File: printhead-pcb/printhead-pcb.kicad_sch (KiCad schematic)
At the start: 30 parts, among them J1 Power, J2 DSCL, J3 DSDA, U1 PCA9615DP, U6 AP7361C-33E

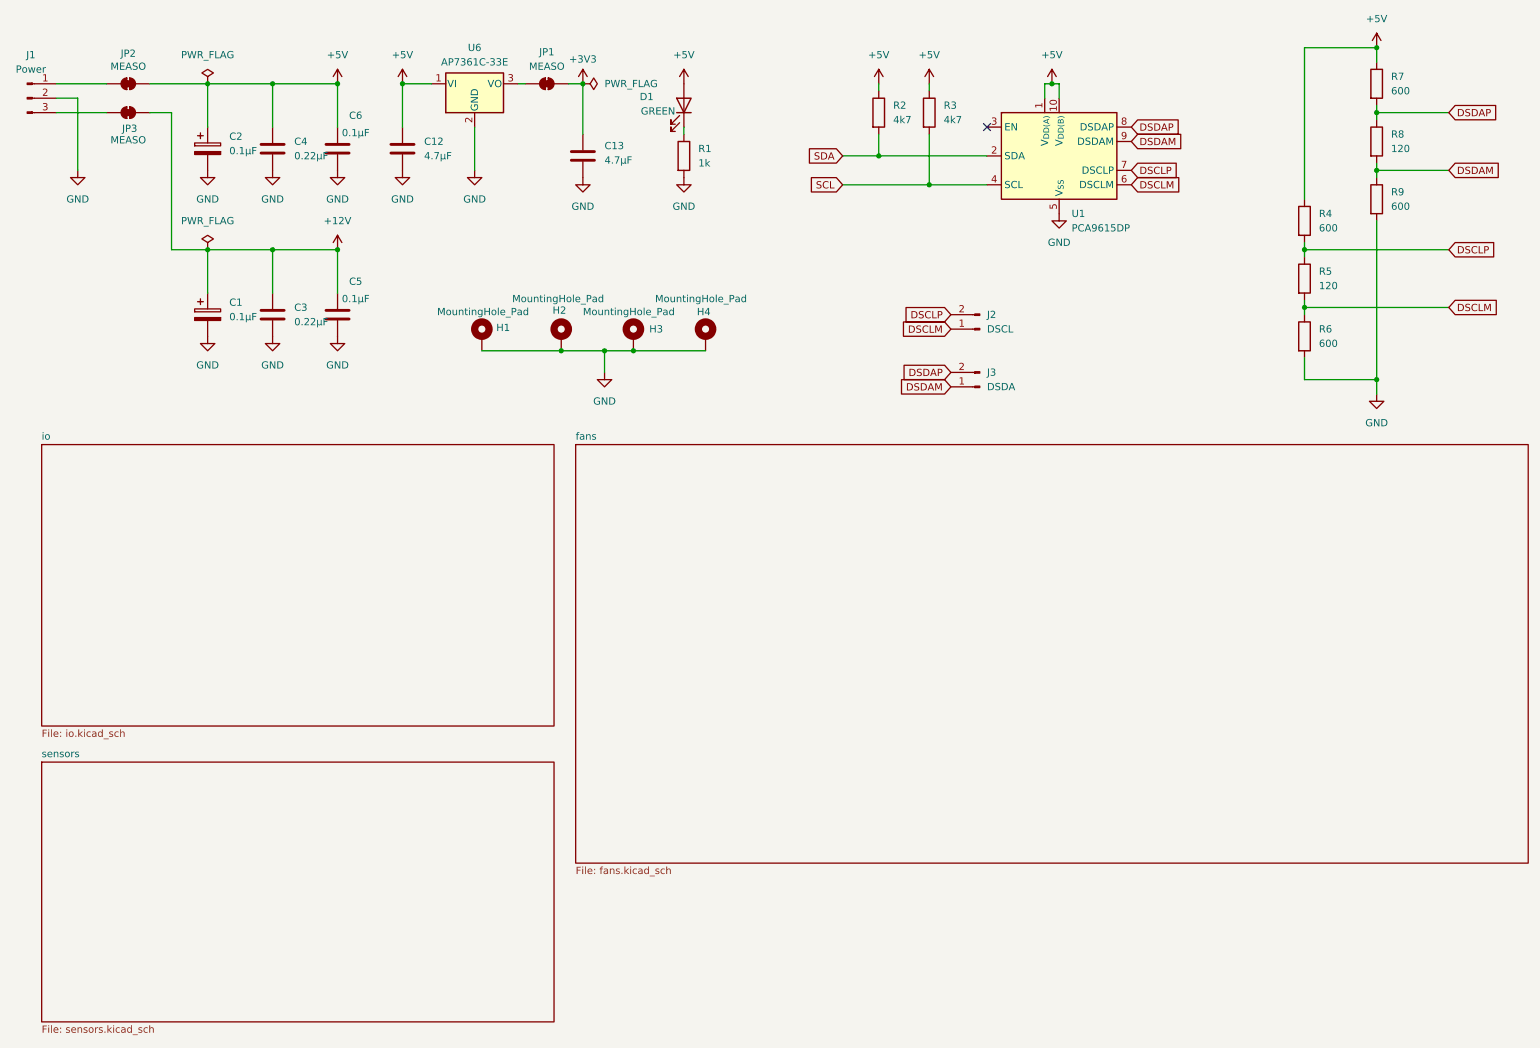
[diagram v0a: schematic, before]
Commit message: added LED Driver and servos
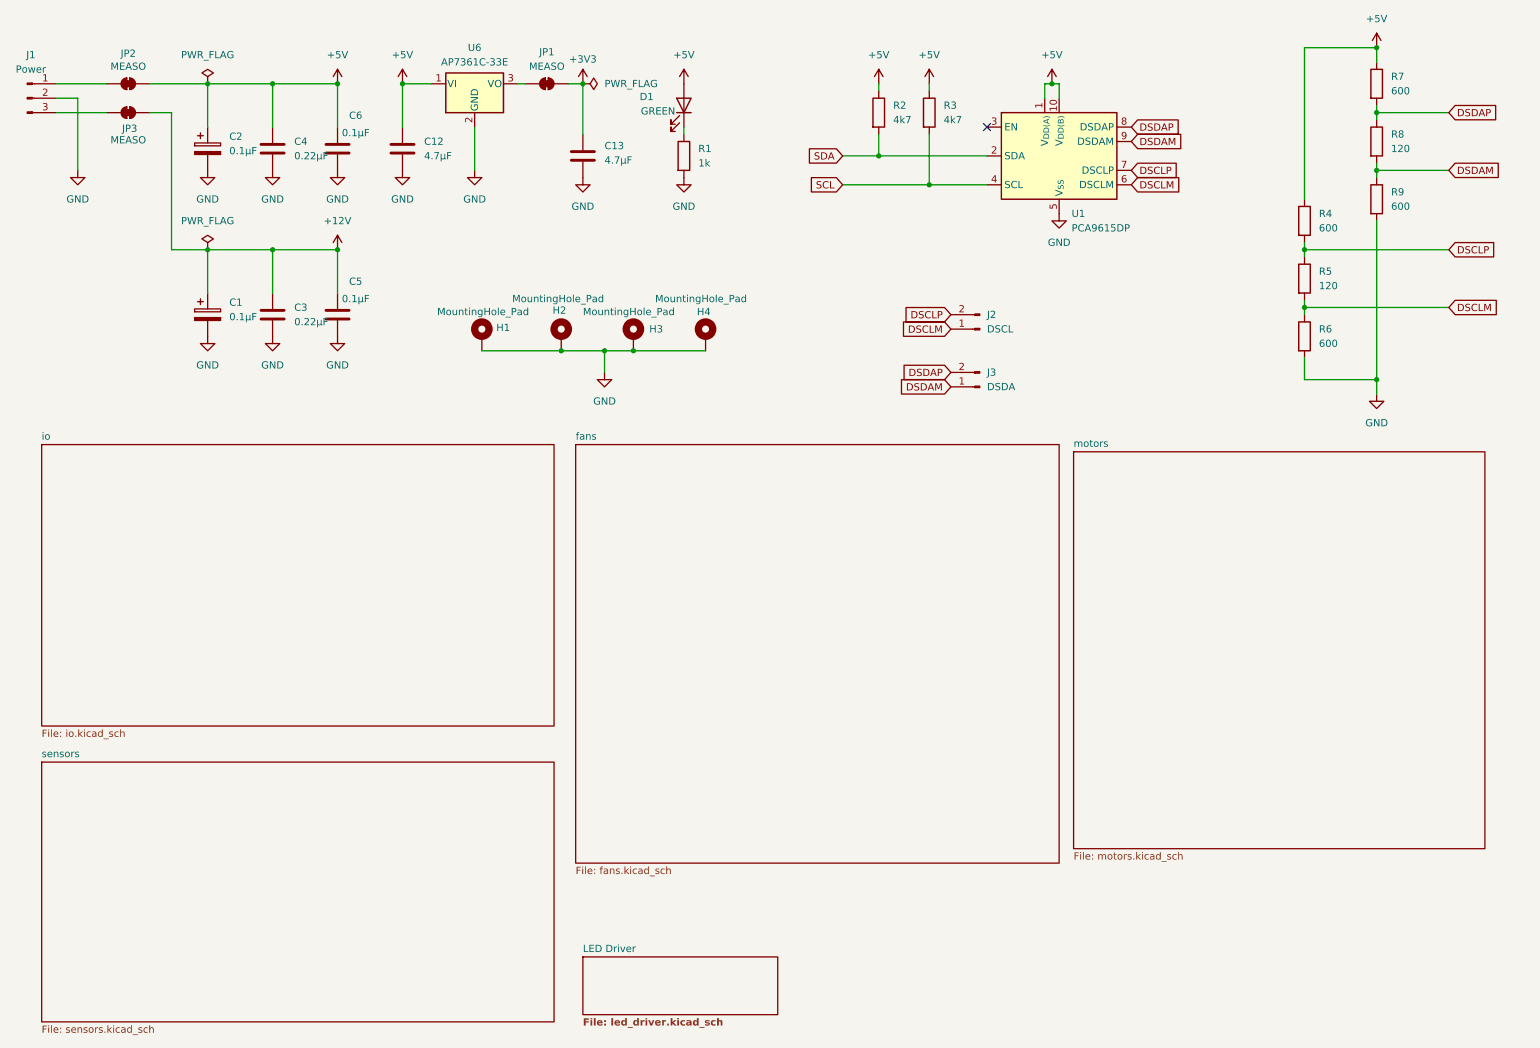
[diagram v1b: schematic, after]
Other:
- added sheet LED Driver (led_driver.kicad_sch)
- added sheet motors (motors.kicad_sch)
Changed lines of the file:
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@@
+	)
+	(sheet
+		(at 201.93 90.17)
+		(size 72.39 69.85)
+		(fields_autoplaced yes)
+		(stroke
+			(width 0.1524)
+			(type solid)
+		)
+		(fill
+			(color 0 0 0 0.0000)
+		)
+		(property "Sheetname" "motors"
+			(at 201.93 89.4584 0)
+			(effects
+				(font
+					(size 1.27 1.27)
+				)
+				(justify left bottom)
+			)
+		)
+		(property "Sheetfile" "motors.kicad_sch"
+			(at 201.93 160.6046 0)
+			(effects
+				(font
+					(size 1.27 1.27)
+				)
+				(justify left top)
+			)
+		)
+		(instances
+			(project "printhead-pcb"
+				(path "/813ad687-b864-44a5-b729-c4edf26b731d"
+					(page "6")
+				)
+			)
+		)
 	)
 	(sheet
 		(at 114.3 88.9)
-		(size 167.64 73.66)
+		(size 85.09 73.66)
 		(fields_autoplaced yes)
 		(stroke
@@
 				)
 			)
+		)
+	)
+	(sheet
+		(at 115.57 179.07)
+		(size 34.29 10.16)
+		(fields_autoplaced yes)
+		(stroke
+			(width 0.1524)
+			(type solid)
+		)
+		(fill
+			(color 0 0 0 0.0000)
+		)
+		(property "Sheetname" "LED Driver"
+			(at 115.57 178.3584 0)
+			(effects
+				(font
+					(size 1.27 1.27)
+				)
+				(justify left bottom)
+			)
+		)
+		(property "Sheetfile" "led_driver.kicad_sch"
+			(at 115.57 189.8146 0)
+			(effects
+				(font
+					(size 1.27 1.27)
+					(bold yes)
+				)
+				(justify left top)
+			)
+		)
+		(instances
+			(project "printhead-pcb"
+				(path "/813ad687-b864-44a5-b729-c4edf26b731d"
+					(page "5")
+				)
+			)

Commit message: Buchse für Netzwerk kabel hinzugefügt, LED Driver überarbeitet, gpio überarbeitet
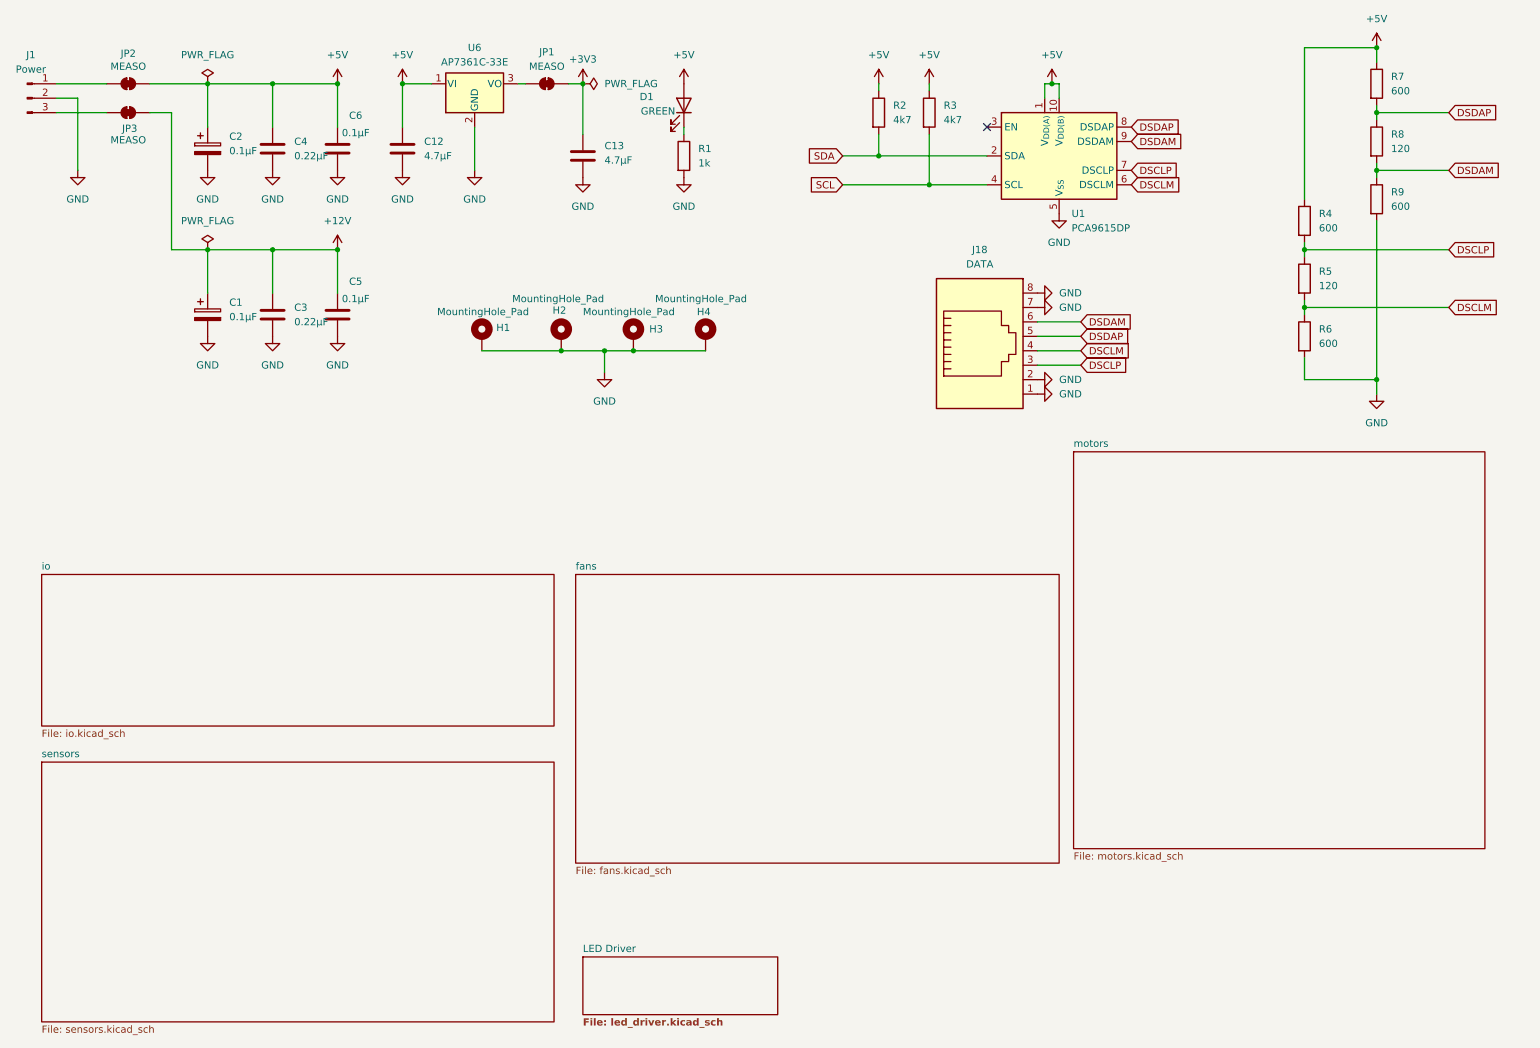
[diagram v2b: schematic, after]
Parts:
- removed J2: DSCL, symbol Connector:Conn_01x02_Pin
- removed J3: DSDA, symbol Connector:Conn_01x02_Pin
- added J18: DATA, Connector_RJ:RJ45_Amphenol_54602-x08_Horizontal, symbol Connector:RJ45
- J1: footprint (none) -> Connector_JST:JST_EH_S3B-EH_1x03_P2.50mm_Horizontal
- JP1, JP2, JP3: footprint (none) -> Jumper:SolderJumper-2_P1.3mm_Bridged_Pad1.0x1.5mm
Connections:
- net DSCLM: now also J18.4
- net DSCLP: now also J18.3
- net DSDAM: now also J18.6
- net DSDAP: now also J18.5
- net GND: now also J18.1, J18.2, J18.7, J18.8

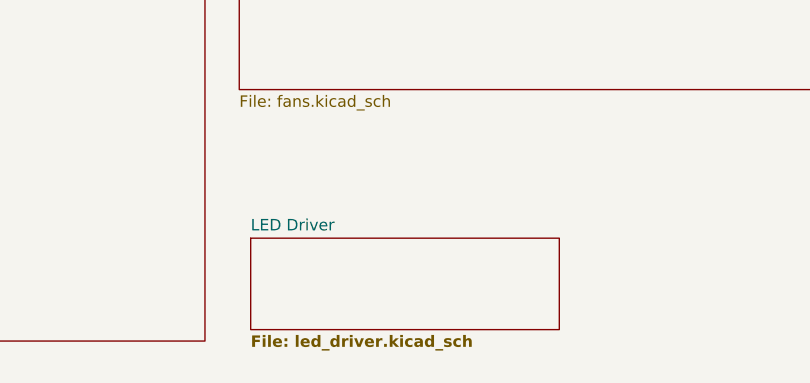
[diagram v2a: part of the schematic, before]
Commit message: removed led driver, added RJ45 (data connector), fan 3. 4. on off
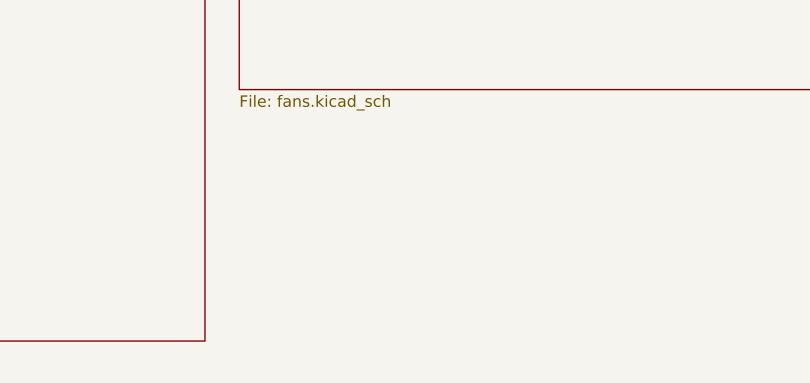
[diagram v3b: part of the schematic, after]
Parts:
- J18: footprint Connector_RJ:RJ45_Amphenol_54602-x08_Horizontal -> Connector_RJ:RJ45_Molex_0855135013_Vertical
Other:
- removed sheet LED Driver
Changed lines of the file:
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@@
 			)
 		)
-		(property "Footprint" "Connector_RJ:RJ45_Amphenol_54602-x08_Horizontal"
+		(property "Footprint" "Connector_RJ:RJ45_Molex_0855135013_Vertical"
 			(at 185.42 71.755 90)
 			(effects
@@
 				)
 			)
-		)
-	)
-	(sheet
-		(at 115.57 179.07)
-		(size 34.29 10.16)
-		(fields_autoplaced yes)
-		(stroke
-			(width 0.1524)
-			(type solid)
-		)
-		(fill
-			(color 0 0 0 0.0000)
-		)
-		(property "Sheetname" "LED Driver"
-			(at 115.57 178.3584 0)
-			(effects
-				(font
-					(size 1.27 1.27)
-				)
-				(justify left bottom)
-			)
-		)
-		(property "Sheetfile" "led_driver.kicad_sch"
-			(at 115.57 189.8146 0)
-			(effects
-				(font
-					(size 1.27 1.27)
-					(bold yes)
-				)
-				(justify left top)
-			)
-		)
-		(instances
-			(project "printhead-pcb"
-				(path "/813ad687-b864-44a5-b729-c4edf26b731d"
-					(page "5")
-				)
-			)

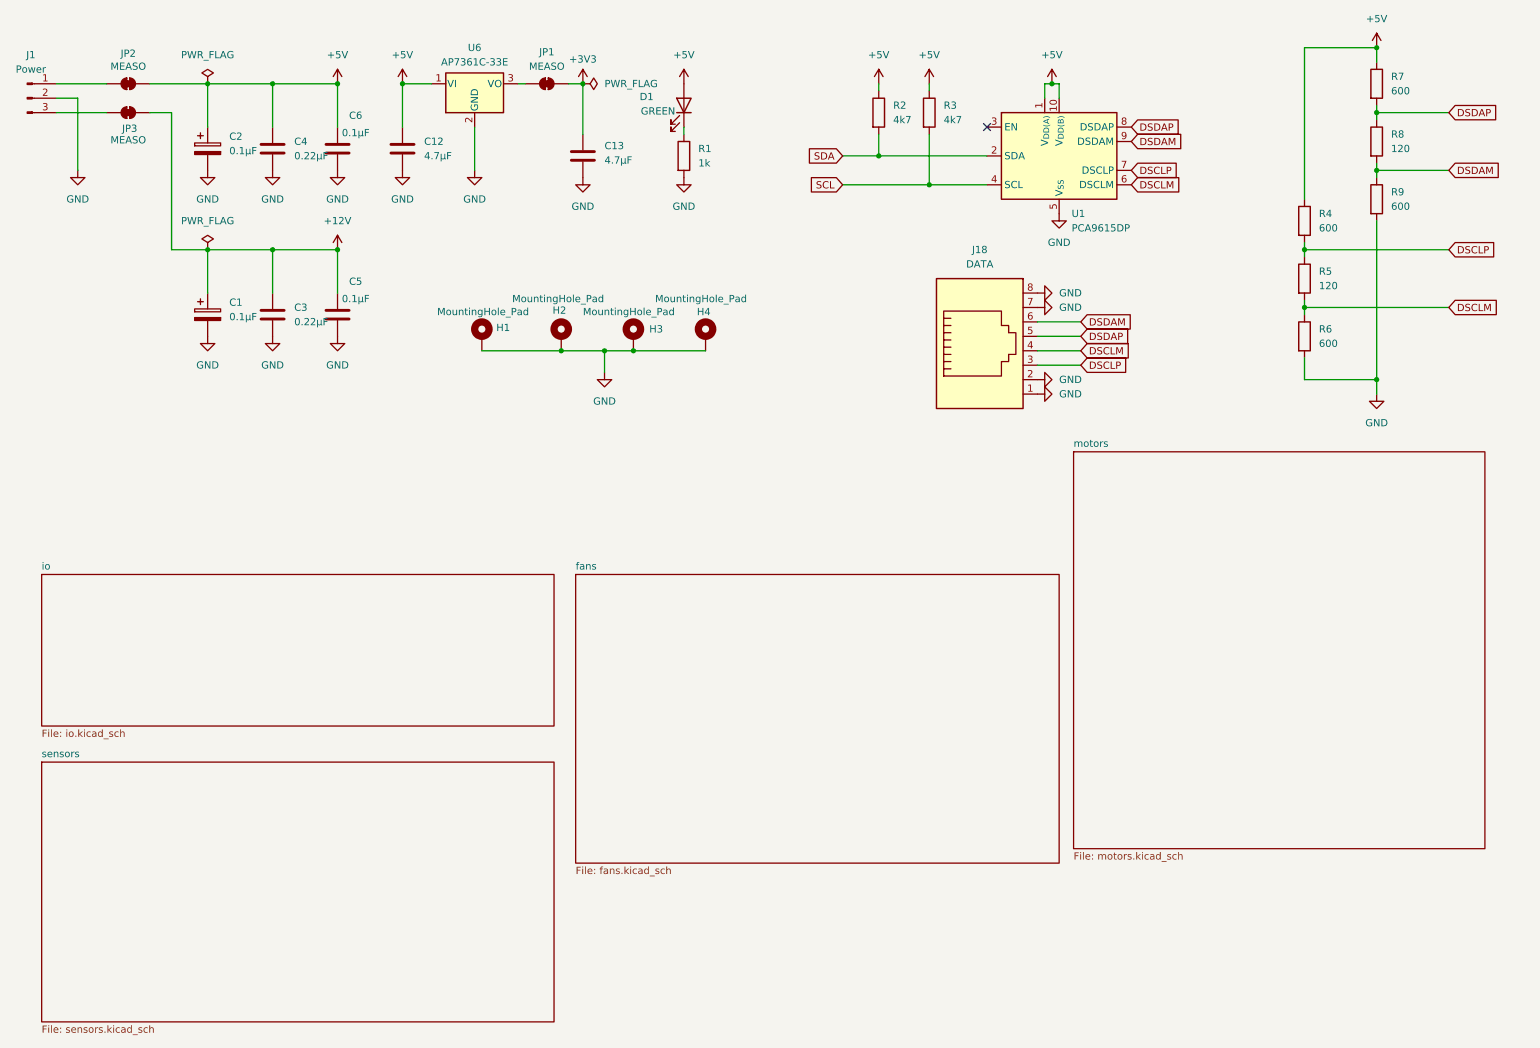
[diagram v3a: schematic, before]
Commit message: Beschriftungen im Schaltplan hinzugefügt
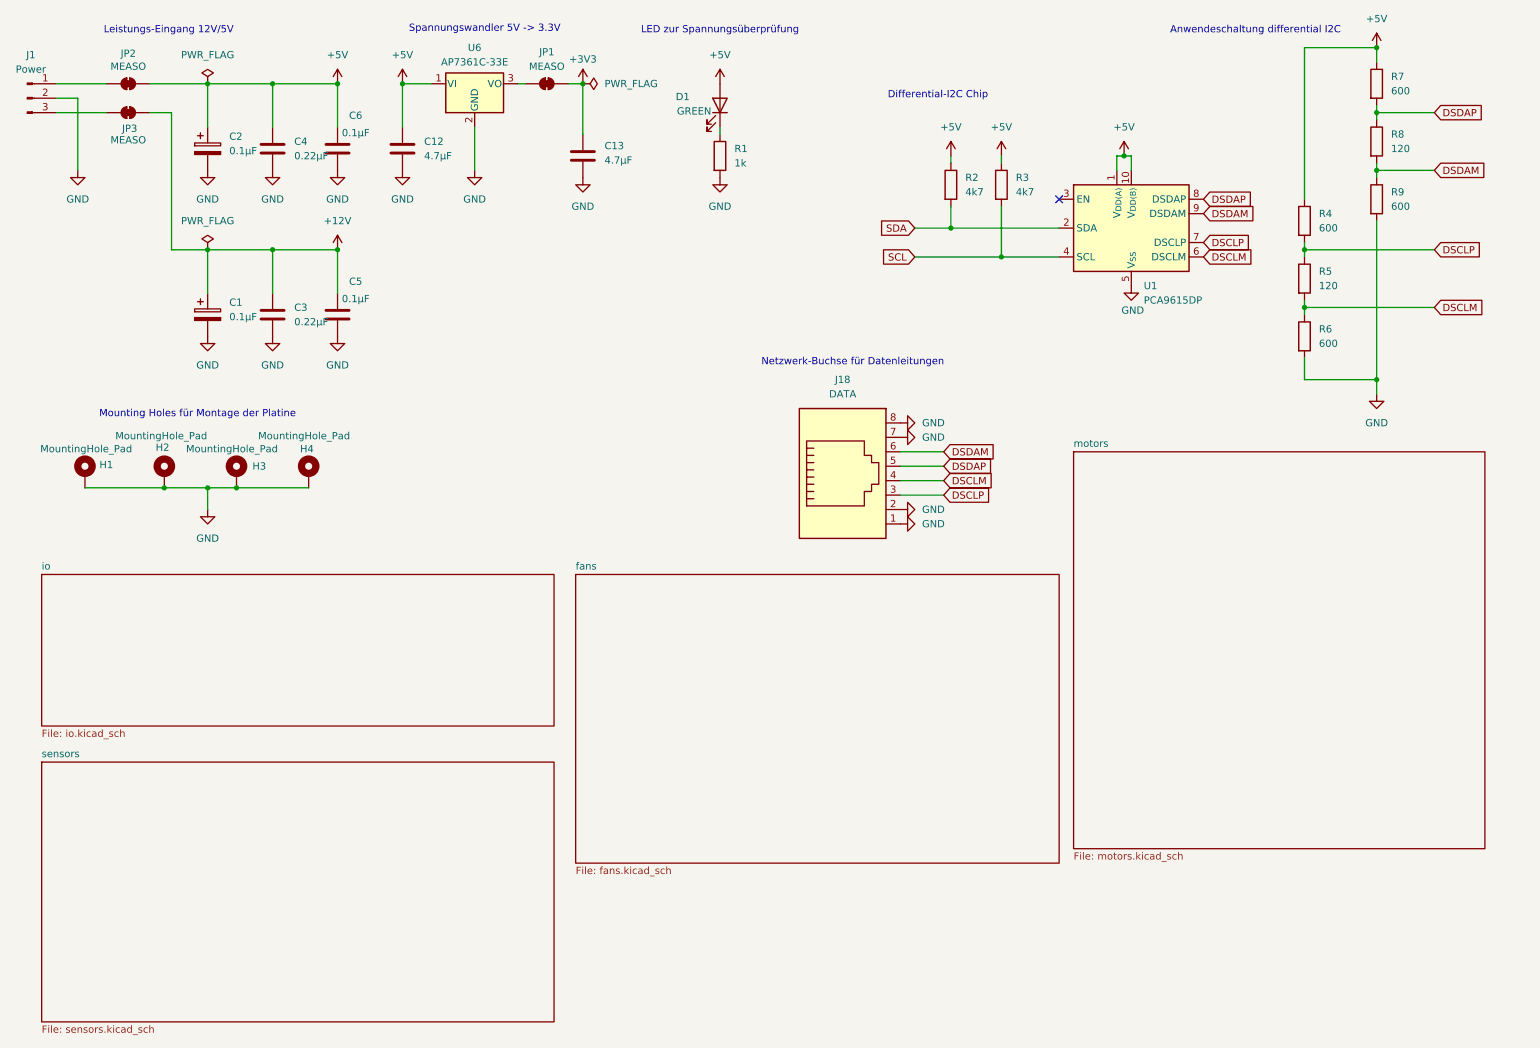
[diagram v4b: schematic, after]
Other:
- note added: "Anwendeschaltung differential I2C"
- note added: "Differential-I2C Chip"
- note added: "LED zur Spannungsüberprüfung"
- note added: "Leistungs-Eingang 12V/5V"
- note added: "Mounting Holes für Montage der Platine"
- note added: "Netzwerk-Buchse für Datenleitungen"
- note added: "Spannungswandler 5V -> 3.3V"
- moved on the sheet: D1, H1, H2, H3, H4, J18, R1, R2, R3, U1
